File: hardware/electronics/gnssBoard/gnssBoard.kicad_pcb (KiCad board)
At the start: 4 copper layers, 22 x 36.8 mm, 49 parts, among them J1 Standoff, J2 M.2_E_Key_PCB_Edge, Q1 DMG1013TQ-7, U1 AP7361E, U2 TXS0104VxRUTR, U3 ZED-F9P, U4 OPA344

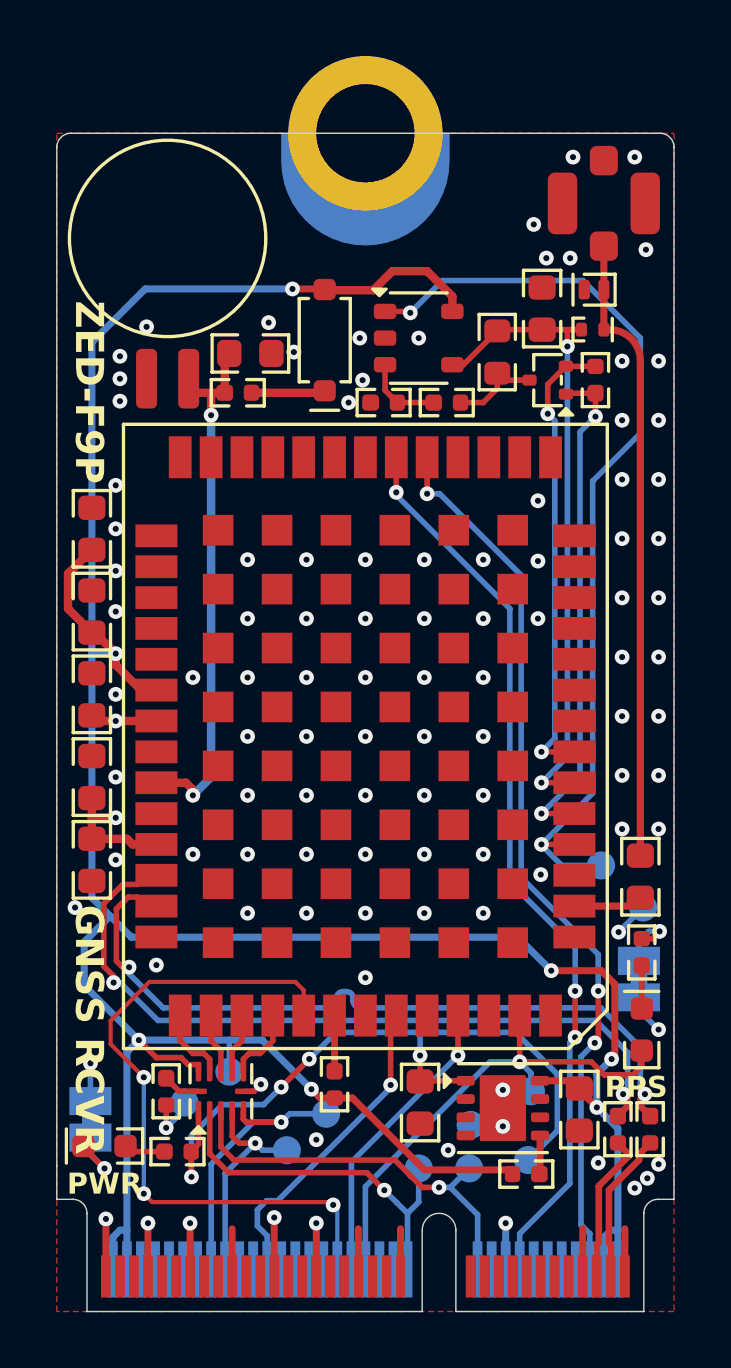
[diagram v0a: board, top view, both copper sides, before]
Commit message: cleaned up board and added fiducials
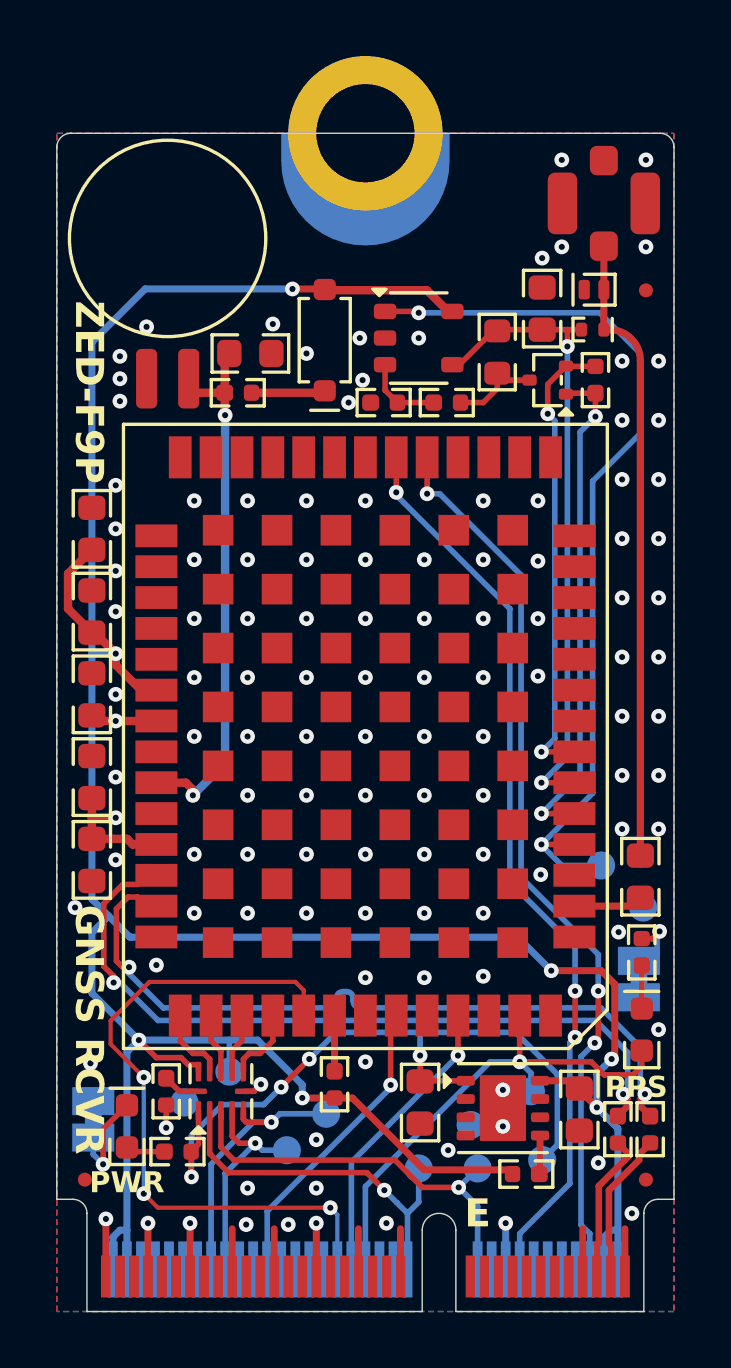
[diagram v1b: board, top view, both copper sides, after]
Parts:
- added REF**: Fiducial_0.5mm_Mask1mm, lib_fp:Fiducial_0.5mm_Mask1mm, F.Cu at (150.0, 115.3)
- added REF**: Fiducial_0.5mm_Mask1mm, lib_fp:Fiducial_0.5mm_Mask1mm, F.Cu at (130.0, 115.3)
- added REF**: Fiducial_0.5mm_Mask1mm, lib_fp:Fiducial_0.5mm_Mask1mm, F.Cu at (150.0, 83.6)
- moved D1 1.06 mm to (131.5, 113.4), turned to -90 degrees
- moved TP2 0.50 mm to (146.3, 114.6)
- moved TP6 0.30 mm to (144.0, 114.9)
- moved JP1 0.10 mm to (130.3, 113.2)
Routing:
- net VSS: track 28.4 -> 21.7 mm, vias 104 -> 118
- net /ANT_DET: track 33.6 -> 32.3 mm
- net Net-(D1-Pad2): track 2.42 -> 3.55 mm
- net +3V3: track 121.2 -> 120.4 mm
- net Net-(JP2-Pad1): track 2.33 -> 1.58 mm
- net /RESET_N: track 11.9 -> 11.4 mm
- added copper zone on B.Cu, net VSS
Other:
- board text added: "E"
- board text added: "Embry-Riddle Aeronautical University Physical Sciences Department Madison Gleydura Master's Thesis 2024-12-23"
- board text removed: "Embry-Riddle Aeronautical University Physical Sciences Department Madison Gleydura Master's Thesis 2024-12-21"

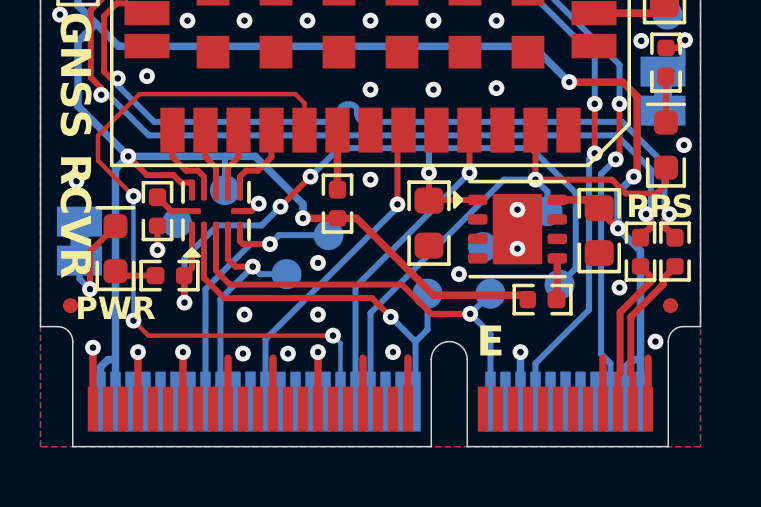
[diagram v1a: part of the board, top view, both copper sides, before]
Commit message: fixed pcb constraints
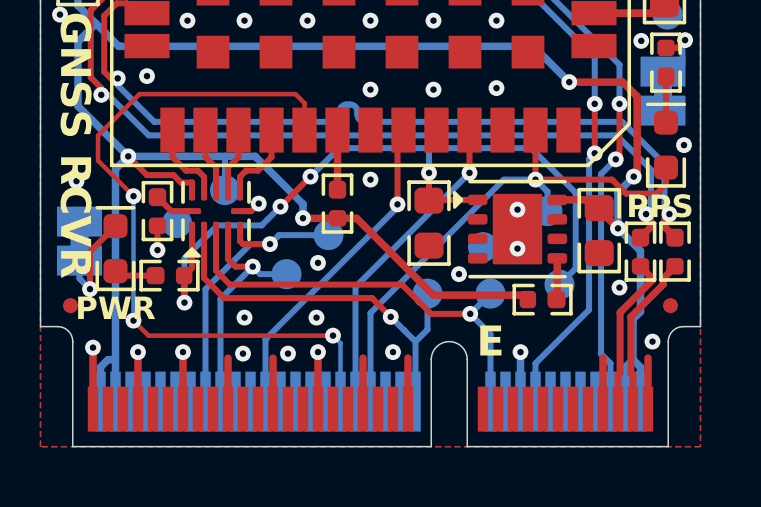
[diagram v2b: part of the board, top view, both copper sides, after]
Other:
- rule pad_to_mask_clearance: 0 -> 0.07
- board text added: "Embry-Riddle Aeronautical University Physical Sciences Department Madison Gleydura Master's Thesis 2025-01-01"
- board text removed: "Embry-Riddle Aeronautical University Physical Sciences Department Madison Gleydura Master's Thesis 2024-12-23"

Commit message: changes from design review
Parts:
- removed R2: 1K, lib_fp:CRCW0402
- removed R3: 10K, lib_fp:CRCW0402
- removed REF** (x3): Fiducial_0.5mm_Mask1mm, lib_fp:Fiducial_0.5mm_Mask1mm
- removed TP8: VSS, lib_fp:TP_1mm
- added C11: 100nF, lib_fp:MLCC0603, F.Cu at (132.9, 114.7)
- added C12: 100nF, lib_fp:MLCC0603, F.Cu at (132.8, 112.5)
- BT1: value ~ -> MS621FE-FL11E
- moved C8 11.8 mm to (130.2, 103.9), turned to -90 degrees
- moved C4 2.95 mm to (130.2, 92.1)
- moved C5 2.95 mm to (130.2, 95.0)
- moved C6 2.95 mm to (130.2, 98.0)
- moved C7 2.95 mm to (130.2, 101.0), turned to 90 degrees
- moved JP1 1.85 mm to (130.3, 111.3)
- moved D1 1.54 mm to (130.2, 114.3)
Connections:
- D1 pad 1: Net-(D1-Pad1) -> +1V8
- U2 pad 12: Net-(U2-OE) -> +1V8
- U3 pad 50: /SAFEBOOT_N -> unconnected-(U3-SAFEBOOT_N-Pad50)
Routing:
- net +1V8: track 25.8 -> 28.5 mm
- net /TX_RDY: track 24.3 -> 22.6 mm
- net Net-(D1-Pad1): track 1.40 -> 0.00 mm
- net Net-(U2-OE): track 1.29 -> 0.00 mm
- net VSS: track 21.7 -> 22.9 mm, vias 118 -> 120
- net Net-(D1-Pad2): track 3.55 -> 2.59 mm
- net +3V3: track 120.3 -> 121.2 mm
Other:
- board text added: "Beveled Edge"
- board text added: "GNSS"
- board text added: "RCVR"
- board text removed: "GNSS RCVR"

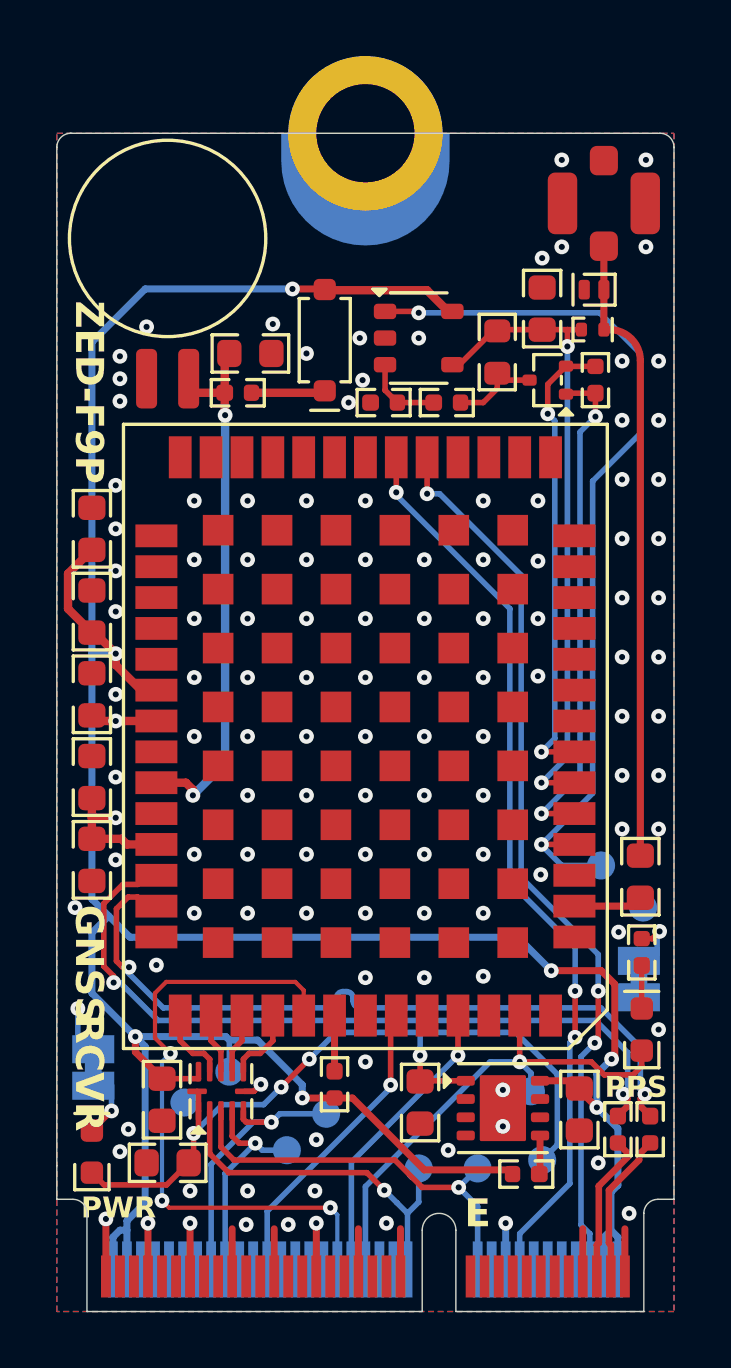
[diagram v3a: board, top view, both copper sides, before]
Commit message: fixed RF trace width, fixed OE, and added decoupling caps to levelshifter
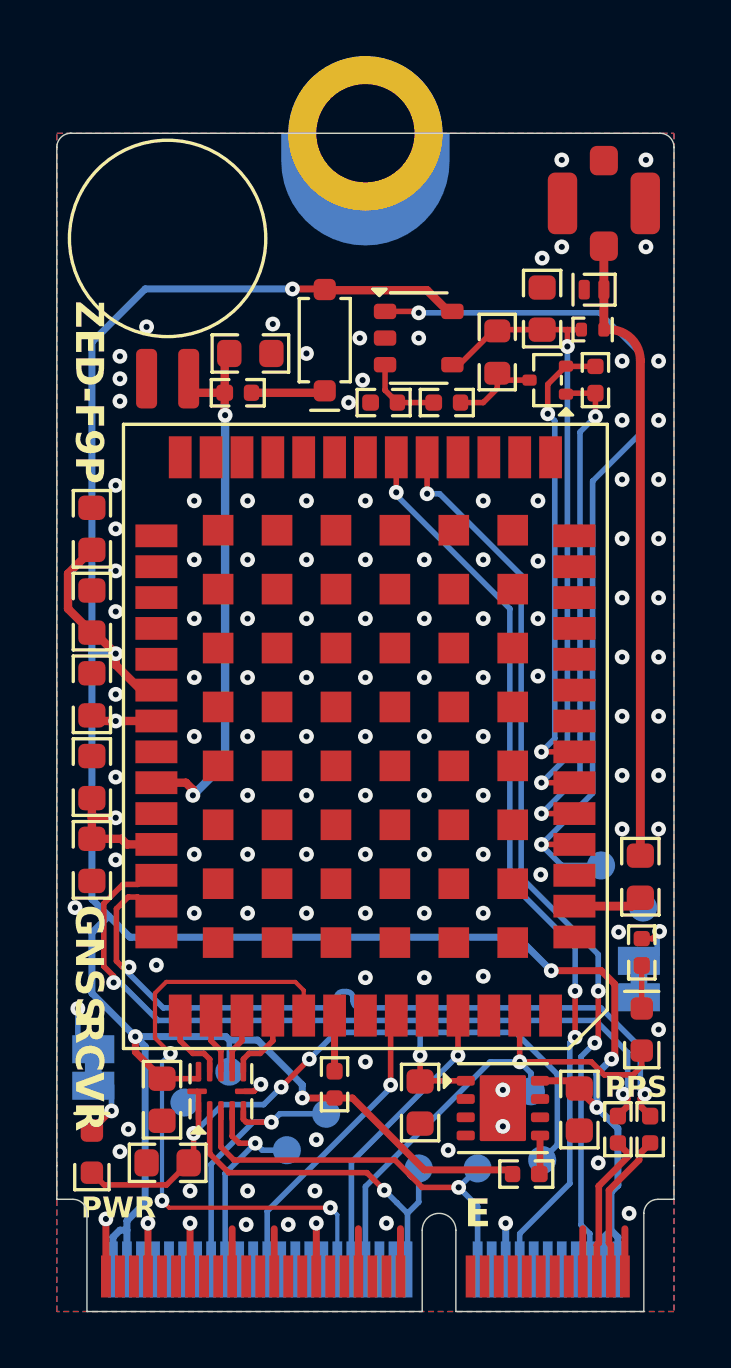
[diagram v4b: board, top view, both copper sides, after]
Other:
- board text added: "Embry-Riddle Aeronautical University Physical Sciences Department Madison Gleydura Master's Thesis 2025-01-14"
- board text removed: "Embry-Riddle Aeronautical University Physical Sciences Department Madison Gleydura Master's Thesis 2025-01-01"
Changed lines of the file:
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@@
 	(title_block
 		(title "U-bolx ZED-F9P M.2 E-Key")
-		(date "2024-12-23")
+		(date "2025-01-14")
 		(comment 2 "PROTOTYPE")
 		(comment 3 "2024")
@@
 		(end 149.8 86.1)
 		(stroke
-			(width 0.2565)
+			(width 0.3175)
 			(type default)
 		)
@@
 		(layer "Edge.Cuts")
 	)
-	(gr_text "Embry-Riddle\nAeronautical University\nPhysical Sciences Department\n\nMadison Gleydura\nMaster's Thesis\n\n2025-01-01"
+	(gr_text "Embry-Riddle\nAeronautical University\nPhysical Sciences Department\n\nMadison Gleydura\nMaster's Thesis\n\n2025-01-14"
 		(at 140 98.1 0)
 		(layer "B.SilkS")
@@
 			(justify mirror)
 		)
-		(render_cache "Embry-Riddle\nAeronautical University\nPhysical Sciences Department\n\nMadison Gleydura\nMaster's Thesis\n\n2025-01-01"
+		(render_cache "Embry-Riddle\nAeronautical University\nPhysical Sciences Department\n\nMadison Gleydura\nMaster's Thesis\n\n2025-01-14"
 			0
 			(polygon
@@
 			(polygon
 				(pts
-					(xy 137.804504 102.315833) (xy 137.81079 102.35267) (xy 137.812221 102.364714) (xy 137.815003 102.402495)
-					(xy 137.815919 102.438582) (xy 137.81587 102.443417) (xy 137.813904 102.480348) (xy 137.813148 102.49025)
-					(xy 137.809874 102.527059) (xy 137.80907 102.532806) (xy 137.801997 102.569191) (xy 137.788808 102.588059)
-					(xy 137.773008 102.564016) (xy 137.766826 102.526509) (xy 137.765418 102.513641) (xy 137.762979 102.475585)
-					(xy 137.762247 102.441696) (xy 137.762263 102.43898) (xy 137.764078 102.401762) (xy 137.764817 102.390512)
-					(xy 137.767742 102.353769) (xy 137.768778 102.345591) (xy 137.776535 102.309622) (xy 137.789907 102.292219)
+					(xy 138.00881 102.692289) (xy 137.839549 102.692289) (xy 137.839549 102.217481) (xy 137.954405 102.341679)
+					(xy 138.026212 102.267124) (xy 137.838633 102.059212) (xy 137.692454 102.059212) (xy 137.692454 102.692289)
+					(xy 137.523194 102.692289) (xy 137.523194 102.82125) (xy 138.00881 102.82125)
 				)
 			)
 			(polygon
 				(pts
-					(xy 137.804932 102.04787) (xy 137.848674 102.053602) (xy 137.887947 102.066211) (xy 137.922751 102.085699)
-					(xy 137.953086 102.112064) (xy 137.978951 102.145307) (xy 137.982839 102.151529) (xy 138.000428 102.185542)
-					(xy 138.014932 102.224394) (xy 138.026349 102.268085) (xy 138.033262 102.306522) (xy 138.038199 102.348056)
-					(xy 138.041161 102.392686) (xy 138.042149 102.440414) (xy 138.042087 102.452558) (xy 138.040606 102.499229)
-					(xy 138.03715 102.542855) (xy 138.031719 102.583435) (xy 138.024313 102.620971) (xy 138.012278 102.663607)
-					(xy 137.997157 102.701485) (xy 137.978951 102.734604) (xy 137.966572 102.752184) (xy 137.938434 102.782156)
-					(xy 137.905787 102.805211) (xy 137.868633 102.821349) (xy 137.82697 102.830572) (xy 137.788808 102.832973)
-					(xy 137.743631 102.829523) (xy 137.702898 102.819172) (xy 137.666609 102.801921) (xy 137.634763 102.77777)
-					(xy 137.607361 102.746717) (xy 137.584402 102.708765) (xy 137.565887 102.663912) (xy 137.551816 102.612159)
-					(xy 137.544904 102.573823) (xy 137.539966 102.53242) (xy 137.537004 102.48795) (xy 137.536017 102.440414)
-					(xy 137.688424 102.440414) (xy 137.688448 102.449133) (xy 137.689268 102.49053) (xy 137.69126 102.528259)
-					(xy 137.695197 102.568694) (xy 137.701922 102.609193) (xy 137.712421 102.646677) (xy 137.726297 102.674967)
-					(xy 137.753809 102.702247) (xy 137.789357 102.71134) (xy 137.81925 102.705025) (xy 137.847895 102.680777)
-					(xy 137.865744 102.646677) (xy 137.867221 102.642505) (xy 137.877344 102.603848) (xy 137.883742 102.562322)
-					(xy 137.887398 102.521007) (xy 137.889155 102.482544) (xy 137.889741 102.440414) (xy 137.889718 102.431672)
-					(xy 137.888898 102.390173) (xy 137.886906 102.35236) (xy 137.882969 102.311848) (xy 137.876243 102.271291)
-					(xy 137.865744 102.233784) (xy 137.853825 102.208588) (xy 137.82715 102.179793) (xy 137.789357 102.169121)
-					(xy 137.759175 102.175436) (xy 137.730324 102.199685) (xy 137.712421 102.233784) (xy 137.710945 102.237957)
-					(xy 137.700821 102.276643) (xy 137.694423 102.318231) (xy 137.690768 102.359628) (xy 137.68901 102.398178)
-					(xy 137.688424 102.440414) (xy 137.536017 102.440414) (xy 137.536078 102.428192) (xy 137.537559 102.381238)
-					(xy 137.541016 102.337382) (xy 137.546447 102.296622) (xy 137.553853 102.25896) (xy 137.565887 102.216237)
-					(xy 137.581008 102.178353) (xy 137.599214 102.145307) (xy 137.611593 102.127826) (xy 137.639732 102.098022)
-					(xy 137.672378 102.075095) (xy 137.709533 102.059047) (xy 137.751195 102.049876) (xy 137.789357 102.047488)
-				)
-			)
-			(polygon
-				(pts
-					(xy 137.377198 102.692289) (xy 137.207937 102.692289) (xy 137.207937 102.217481) (xy 137.322793 102.341679)
-					(xy 137.3946 102.267124) (xy 137.207021 102.059212) (xy 137.060842 102.059212) (xy 137.060842 102.692289)
-					(xy 136.891582 102.692289) (xy 136.891582 102.82125) (xy 137.377198 102.82125)
+					(xy 137.421345 102.511489) (xy 137.421345 102.657118) (xy 137.117812 102.657118) (xy 137.117812 102.82125)
+					(xy 136.972732 102.82125) (xy 136.972732 102.657118) (xy 136.888651 102.657118) (xy 136.888651 102.528158)
+					(xy 136.972732 102.528158) (xy 137.117812 102.528158) (xy 137.311069 102.528158) (xy 137.117812 102.231403)
+					(xy 137.117812 102.528158) (xy 136.972732 102.528158) (xy 136.972732 102.059212) (xy 137.131001 102.059212)
 				)
 			)
@@
 		(start 148.5 83.6)
 		(end 148.5 82.025)
-		(width 0.2565)
+		(width 0.3175)
 		(layer "F.Cu")
 		(net 2)
@@
 		(start 149.8 103.75)
 		(end 149.8 86.1)
-		(width 0.2565)
+		(width 0.3175)
 		(layer "F.Cu")
 		(net 2)
@@
 		(start 148.5 85)
 		(end 148.5 83.6)
-		(width 0.2565)
+		(width 0.3175)
 		(layer "F.Cu")
 		(net 2)
@@
 		(start 149.499999 105.550001)
 		(end 149.8 105.25)
-		(width 0.2565)
+		(width 0.3175)
 		(layer "F.Cu")
 		(net 6)
@@
 		(start 147.45 105.550001)
 		(end 149.499999 105.550001)
-		(width 0.2565)
+		(width 0.3175)
 		(layer "F.Cu")
 		(net 6)

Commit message: fixed rf/usb trace width
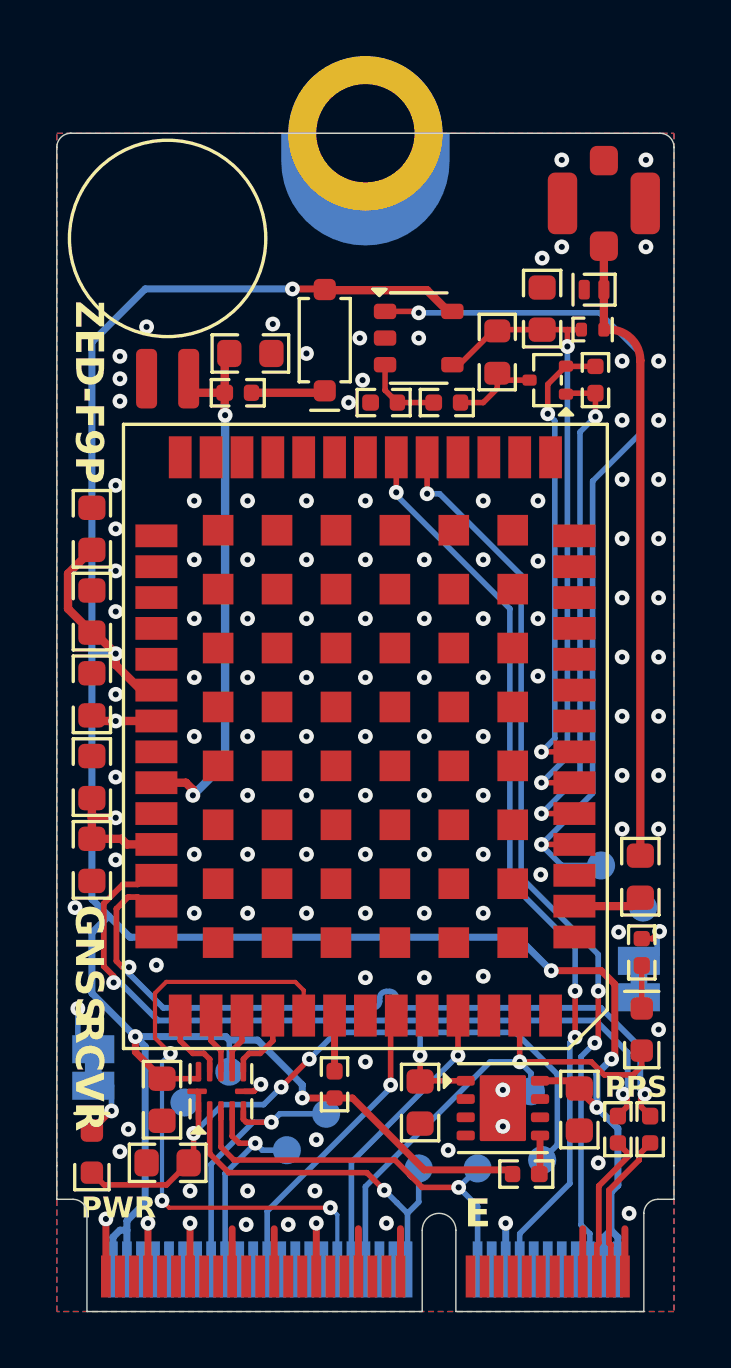
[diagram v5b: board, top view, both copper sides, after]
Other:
- board text added: "Board thickness is 0.8mm 4-Layer Beveled Edge (20deg) ENIG Finish w/ Hard Gold Fingers (ENIG for prototypeing) Dielectric/Prepreg: S1000H/S1000HB"
- board text removed: "Board thickness is 0.8mm 4-Layer Beveled Edge ENIG Finish w/ Hard Gold Fingers"
